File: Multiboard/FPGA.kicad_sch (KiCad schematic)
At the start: 0 parts

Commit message: Implemented FTDI in schematic
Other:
- added sheet FTDI (FT2232HL.kicad_sch)
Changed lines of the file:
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@@
 	(generator_version "9.0")
 	(paper "A4")
+	(sheet
+		(at 24.13 98.806)
+		(size 49.53 90.424)
+		(exclude_from_sim no)
+		(in_bom yes)
+		(on_board yes)
+		(dnp no)
+		(fields_autoplaced yes)
+		(stroke
+			(width 0.1524)
+			(type solid)
+		)
+		(fill
+			(color 0 0 0 0.0000)
+		)
+		(property "Sheetname" "FTDI"
+			(at 24.13 98.0944 0)
+			(effects
+				(font
+					(size 1.27 1.27)
+				)
+				(justify left bottom)
+			)
+		)
+		(property "Sheetfile" "FT2232HL.kicad_sch"
+			(at 24.13 189.8146 0)
+			(effects
+				(font
+					(size 1.27 1.27)
+				)
+				(justify left top)
+			)
+		)
+		(instances
+			(project "Multiboard"
+				(path "/9ed4a389-3aa7-41f1-b239-280eb7f09ef1/a1879700-d4ae-4f4f-b9ed-53e5618d969d"
+					(page "5")
+				)
+			)
+		)
+	)
 )

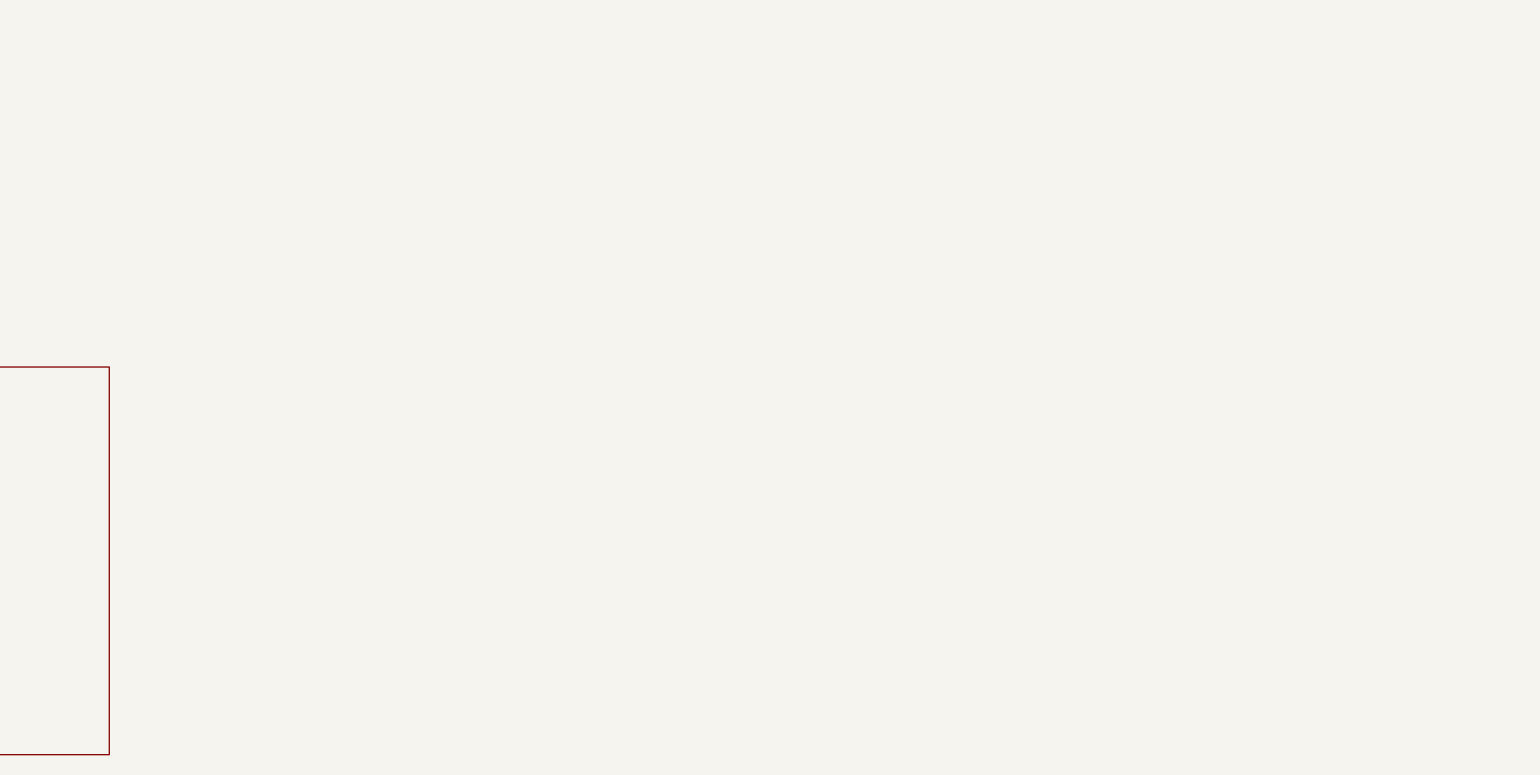
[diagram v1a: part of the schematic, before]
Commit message: added and wired banks to the fpga schematic
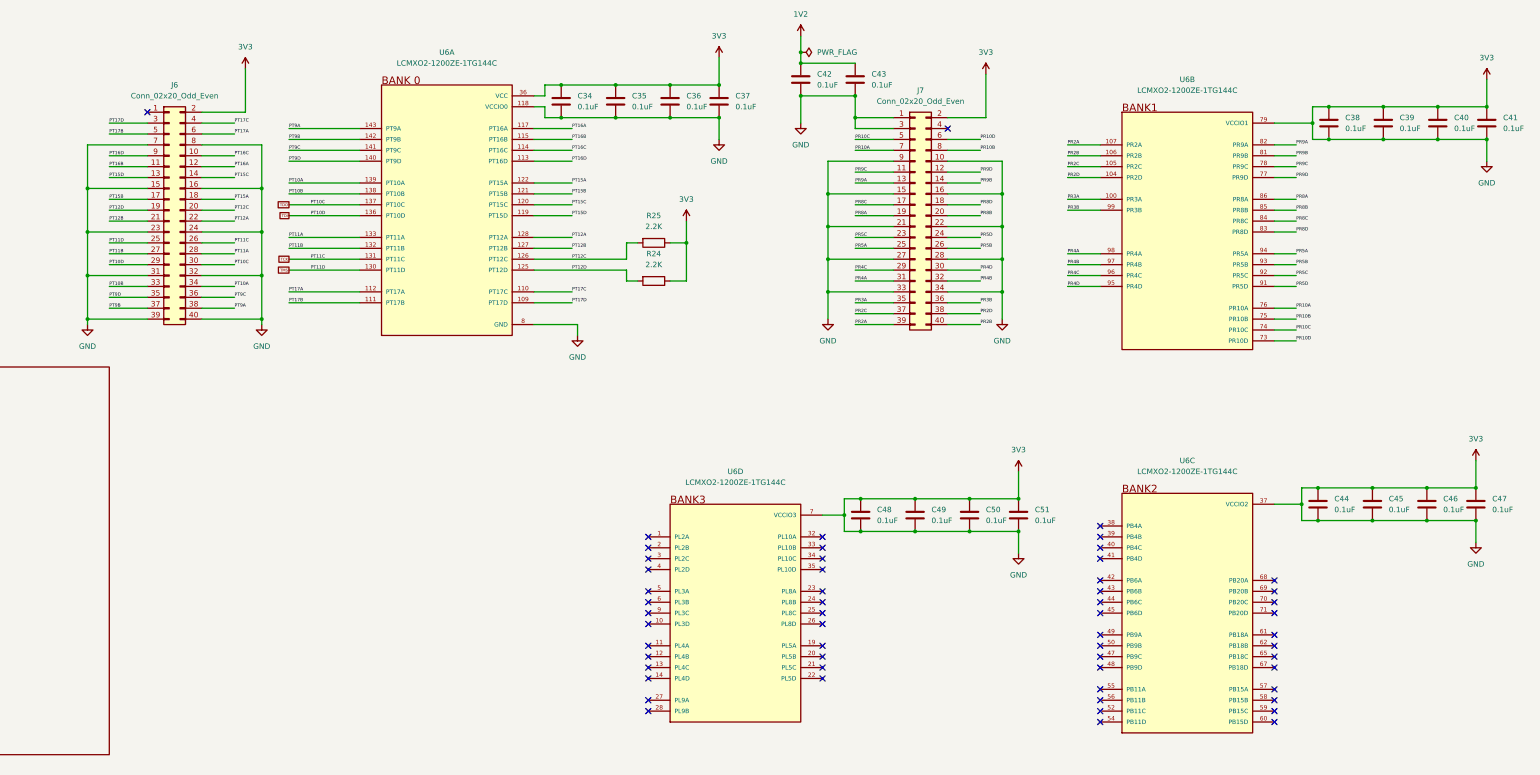
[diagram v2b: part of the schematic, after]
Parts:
- added C34, C35, C36, C37, C38, C39, C40, C41, C42, C43, C44, C45, C46, C47, C48, C49, C50, C51: 0.1uF, symbol Device:C
- added J6, J7: Conn_02x20_Odd_Even, Connector_IDC:IDC-Header_2x20_P2.54mm_Vertical, symbol Connector_Generic:Conn_02x20_Odd_Even
- added R24, R25: 2.2K, symbol Device:R
- added U6: LCMXO2-1200ZE-1TG144C, LCMXO2-1200ZE-1TG144C:QFP50P2200X2200X160-144N, symbol LCMXO2-1200ZE-1TG144C:LCMXO2-1200ZE-1TG144C
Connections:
- new net 1V2: C42.1, C43.1
- new net 3V3: C34.1, C34.2, C35.1, C35.2, C36.1, C36.2, C37.1, C37.2, C38.1, C38.2, C39.1, C39.2, C40.1, C40.2, C41.1, C41.2, C42.2, C43.2, C44.1, C44.2, C45.1, C45.2, C46.1, C46.2, C47.1, C47.2, C48.1, C48.2, C49.1, C49.2, C50.1, C50.2, C51.1, C51.2, J6.15 (Pin_15), J6.16 (Pin_16), J6.2 (Pin_2), J6.23 (Pin_23), J6.24 (Pin_24), J6.31 (Pin_31), J6.32 (Pin_32), J6.39 (Pin_39), J6.40 (Pin_40), J6.7 (Pin_7), J6.8 (Pin_8), J7.1 (Pin_1), J7.10 (Pin_10), J7.15 (Pin_15), J7.16 (Pin_16), J7.2 (Pin_2), J7.21 (Pin_21), J7.22 (Pin_22), J7.27 (Pin_27), J7.28 (Pin_28), J7.3 (Pin_3), J7.33 (Pin_33), J7.34 (Pin_34), J7.9 (Pin_9), R24.1, R25.1, U6.101 (GND), U6.102 (VCCIO1), U6.108 (VCC), U6.116 (GND), U6.118 (VCCIO0), U6.123 (VCCIO0), U6.124 (GND), U6.134 (GND), U6.135 (VCCIO0), U6.144 (VCC), U6.16 (VCCIO3), U6.18 (GND), U6.29 (GND), U6.30 (VCCIO3), U6.36 (VCC), U6.37 (VCCIO2), U6.46 (GND), U6.51 (VCCIO2), U6.53 (GND), U6.64 (GND), U6.66 (VCCIO2), U6.7 (VCCIO3), U6.72 (VCC), U6.79 (VCCIO1), U6.8 (GND), U6.80 (GND), U6.88 (VCCIO1), U6.90 (GND)
- new net PR10A: J7.7 (Pin_7), U6.76 (PR10A)
- new net PR10B: J7.8 (Pin_8), U6.75 (PR10B)
- new net PR10C: J7.5 (Pin_5), U6.74 (PR10C)
- new net PR10D: J7.6 (Pin_6), U6.73 (PR10D)
- new net PR2A: J7.39 (Pin_39), U6.107 (PR2A)
- new net PR2B: J7.40 (Pin_40), U6.106 (PR2B)
- new net PR2C: J7.37 (Pin_37), U6.105 (PR2C)
- new net PR2D: J7.38 (Pin_38), U6.104 (PR2D)
- new net PR3A: J7.35 (Pin_35), U6.100 (PR3A)
- new net PR3B: J7.36 (Pin_36), U6.99 (PR3B)
- new net PR4A: J7.31 (Pin_31), U6.98 (PR4A)
- new net PR4B: J7.32 (Pin_32), U6.97 (PR4B)
- new net PR4C: J7.29 (Pin_29), U6.96 (PR4C)
- new net PR4D: J7.30 (Pin_30), U6.95 (PR4D)
- new net PR5A: J7.25 (Pin_25), U6.94 (PR5A)
- new net PR5B: J7.26 (Pin_26), U6.93 (PR5B)
- new net PR5C: J7.23 (Pin_23), U6.92 (PR5C)
- new net PR5D: J7.24 (Pin_24), U6.91 (PR5D)
- new net PR8A: J7.19 (Pin_19), U6.86 (PR8A)
- new net PR8B: J7.20 (Pin_20), U6.85 (PR8B)
- new net PR8C: J7.17 (Pin_17), U6.84 (PR8C)
- new net PR8D: J7.18 (Pin_18), U6.83 (PR8D)
- new net PR9A: J7.13 (Pin_13), U6.82 (PR9A)
- new net PR9B: J7.14 (Pin_14), U6.81 (PR9B)
- new net PR9C: J7.11 (Pin_11), U6.78 (PR9C)
- new net PR9D: J7.12 (Pin_12), U6.77 (PR9D)
- new net PT10A: J6.34 (Pin_34), U6.139 (PT10A)
- new net PT10B: J6.33 (Pin_33), U6.138 (PT10B)
- new net PT11A: J6.28 (Pin_28), U6.133 (PT11A)
- new net PT11B: J6.27 (Pin_27), U6.132 (PT11B)
- new net PT12A: J6.22 (Pin_22), U6.128 (PT12A)
- new net PT12B: J6.21 (Pin_21), U6.127 (PT12B)
- new net PT12C: J6.20 (Pin_20), R25.2, U6.126 (PT12C)
- new net PT12D: J6.19 (Pin_19), R24.2, U6.125 (PT12D)
- new net PT15A: J6.18 (Pin_18), U6.122 (PT15A)
- new net PT15B: J6.17 (Pin_17), U6.121 (PT15B)
- new net PT15C: J6.14 (Pin_14), U6.120 (PT15C)
- new net PT15D: J6.13 (Pin_13), U6.119 (PT15D)
- new net PT16A: J6.12 (Pin_12), U6.117 (PT16A)
- new net PT16B: J6.11 (Pin_11), U6.115 (PT16B)
- new net PT16C: J6.10 (Pin_10), U6.114 (PT16C)
- new net PT16D: J6.9 (Pin_9), U6.113 (PT16D)
- new net PT17A: J6.6 (Pin_6), U6.112 (PT17A)
- new net PT17B: J6.5 (Pin_5), U6.111 (PT17B)
- new net PT17C: J6.4 (Pin_4), U6.110 (PT17C)
- new net PT17D: J6.3 (Pin_3), U6.109 (PT17D)
- new net PT9A: J6.38 (Pin_38), U6.143 (PT9A)
- new net PT9B: J6.37 (Pin_37), U6.142 (PT9B)
- new net PT9C: J6.36 (Pin_36), U6.141 (PT9C)
- new net PT9D: J6.35 (Pin_35), U6.140 (PT9D)
- new net TCK: J6.26 (Pin_26), U6.131 (PT11C)
- new net TDI: J6.29 (Pin_29), U6.136 (PT10D)
- new net TDO: J6.30 (Pin_30), U6.137 (PT10C)
- new net TMS: J6.25 (Pin_25), U6.130 (PT11D)
- no-connect marks 0 -> 56

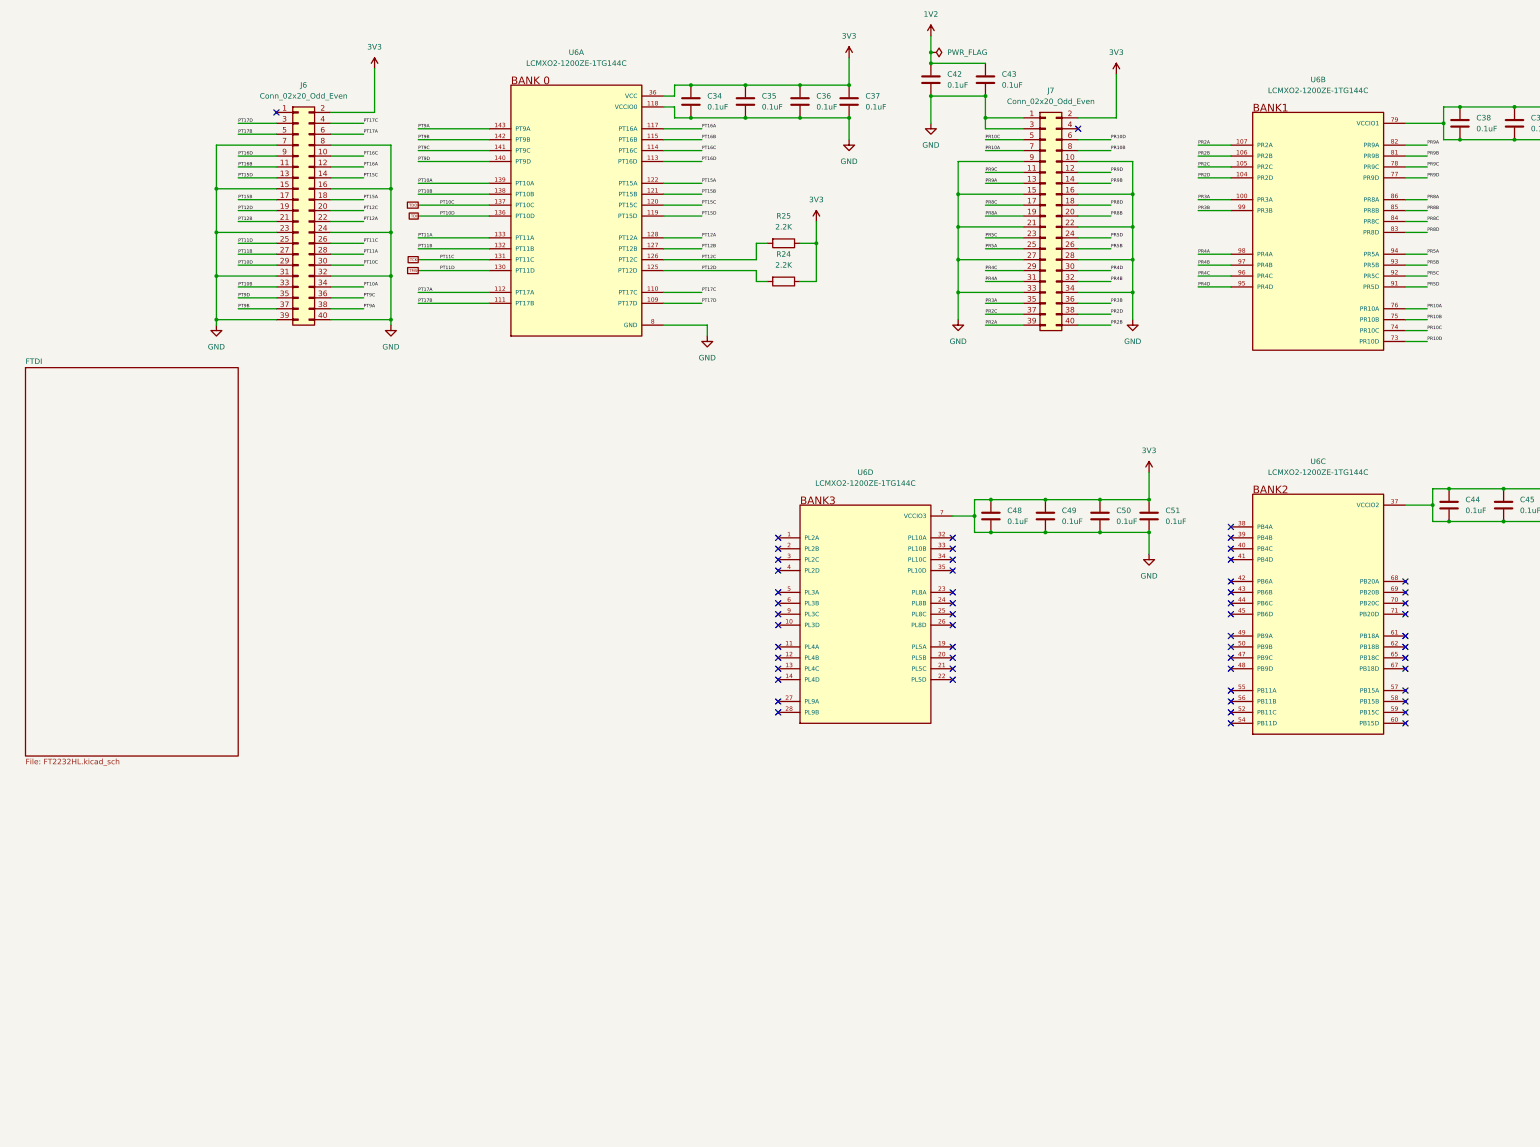
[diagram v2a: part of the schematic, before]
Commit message: completed v1 FPGA schematic
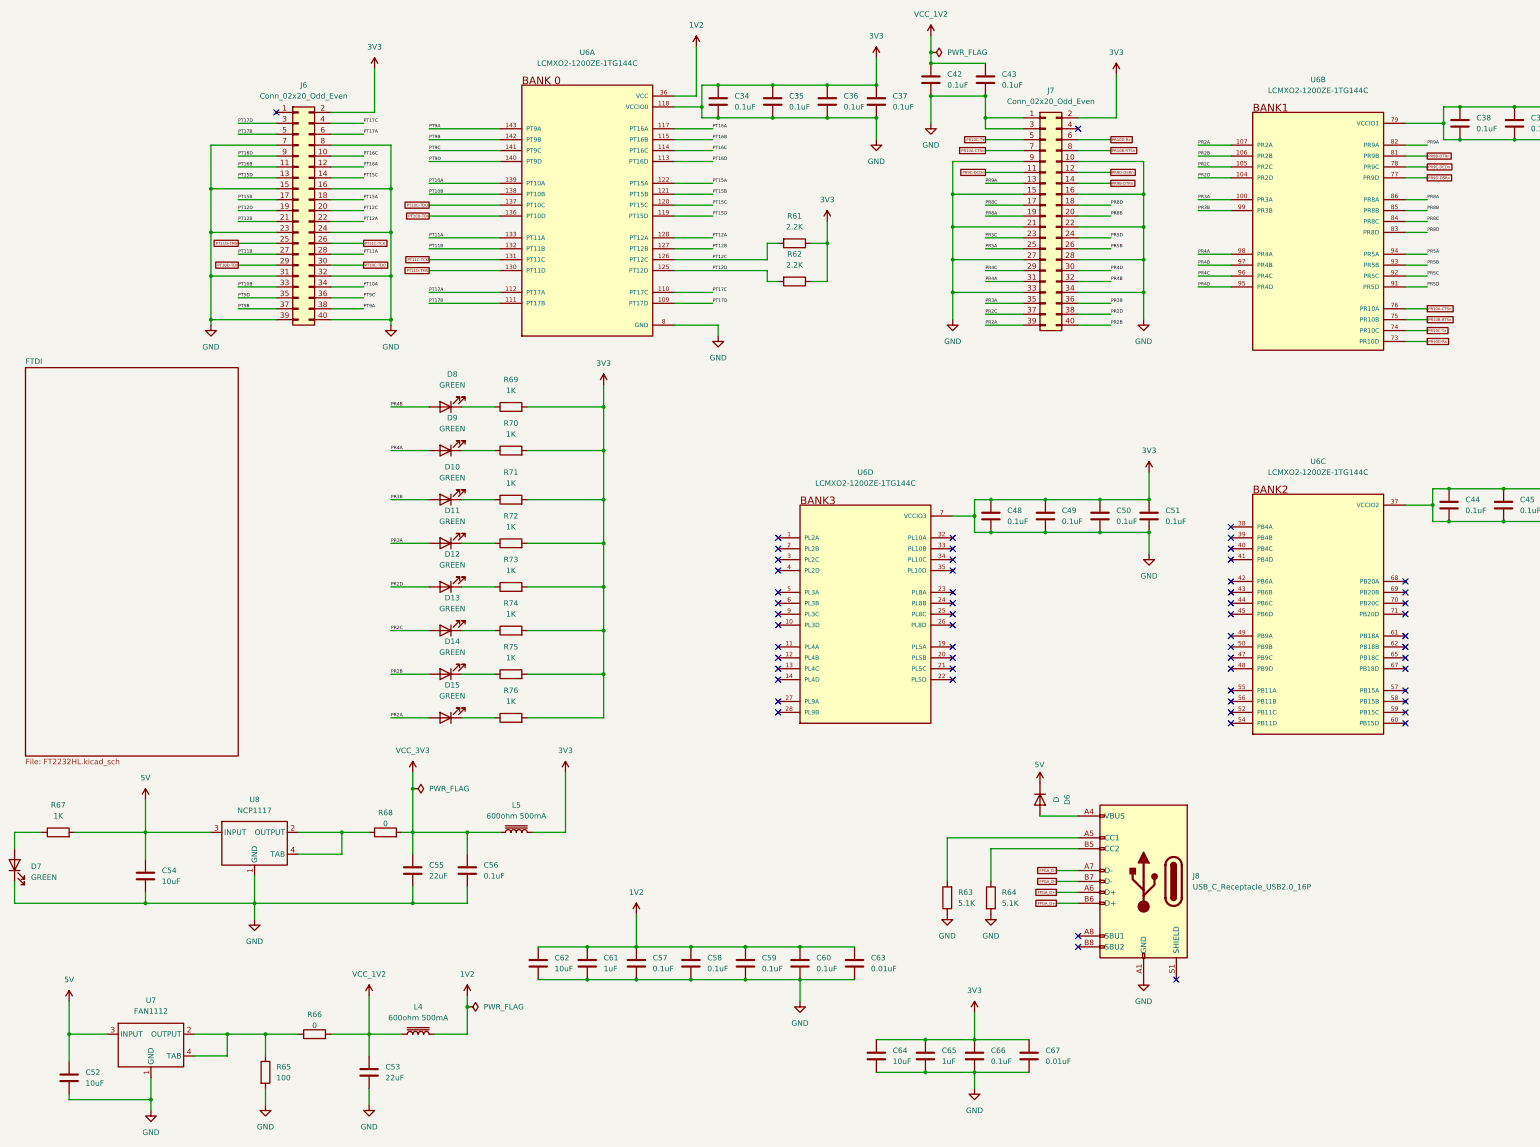
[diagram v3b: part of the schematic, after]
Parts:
- added C52, C54, C62, C64: 10uF, symbol Device:C
- added C53, C55: 22uF, symbol Device:C
- added C56, C57, C58, C59, C60, C66: 0.1uF, symbol Device:C
- added C61, C65: 1uF, symbol Device:C
- added C63, C67: 0.01uF, symbol Device:C
- added D10, D11, D12, D13, D14, D15, D7, D8, D9: GREEN, symbol Device:LED
- added D6: D, Diode_SMD:D_0603_1608Metric_Pad1.05x0.95mm_HandSolder, symbol Device:D
- added J8: USB_C_Receptacle_USB2.0_16P, Connector_USB:USB_C_Receptacle_G-Switch_GT-USB-7010ASV, symbol Connector:USB_C_Receptacle_USB2.0_16P
- added L4, L5: 600ohm 500mA, Inductor_SMD:L_0603_1608Metric_Pad1.05x0.95mm_HandSolder, symbol Device:L_Iron
- added R63, R64: 5.1K, symbol Device:R
- added R65: 100, symbol Device:R
- added R66, R68: 0, symbol Device:R
- added R67, R69, R70, R71, R72, R73, R74, R75, R76: 1K, symbol Device:R
- added U7: FAN1112, symbol FPGA_LDO:FPGA_LDO
- added U8: NCP1117, symbol FPGA_LDO:FPGA_LDO
- renumbered R25 to R61, R24 to R62
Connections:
- net 1V2: now also U6.108 (VCC), U6.144 (VCC), U6.36 (VCC), U6.72 (VCC), C57.1, C58.1, C59.1, C60.1, C61.1, C62.1, C63.1, L4.2; no longer C42.1, C43.1
- net 3V3: now also C52.2, C53.2, C54.2, C55.2, C56.2, C57.2, C58.2, C59.2, C60.2, C61.2, C62.2, C63.2, C64.1, C64.2, C65.1, C65.2, C66.1, C66.2, C67.1, C67.2, D7.1 (K), J8.A1 (GND), J8.A12 (GND), J8.B1 (GND), J8.B12 (GND), L5.2, R63.1, R64.2, R65.2, R69.2, R70.2, R71.2, R72.2, R73.2, R74.2, R75.2, R76.2, U7.1 (GND), U8.1 (GND); no longer U6.108 (VCC), U6.144 (VCC), U6.36 (VCC), U6.72 (VCC)
- net PR2A: now also D15.2 (A)
- net PR2B: now also D14.2 (A)
- net PR2C: now also D13.2 (A)
- net PR2D: now also D12.2 (A)
- net PR3A: now also D11.2 (A)
- net PR3B: now also D10.2 (A)
- net PR4A: now also D9.2 (A)
- net PR4B: now also D8.2 (A)
- net PR10A renamed PR10A-CTSn
- net PR10B renamed PR10B-RTSn
- net PR10C renamed PR10C-Tx
- net PR10D renamed PR10D-Rx
- net PR9B renamed PR9B-DTRn
- net PR9C renamed PR9C-DCDn
- net PR9D renamed PR9D-DSRn
- net TCK renamed PT11C-TCK
- net TDI renamed PT10D-TDI
- net TDO renamed PT10C-TDO
- net TMS renamed PT11D-TMS
- new net: D15.1 (K), R76.1
- new net: D13.1 (K), R74.1
- new net: R65.1, R66.1, U7.2 (OUTPUT), U7.4 (TAB)
- new net: D9.1 (K), R70.1
- new net: D6.2 (A), J8.A4 (VBUS), J8.A9 (VBUS), J8.B4 (VBUS), J8.B9 (VBUS)
- new net: D10.1 (K), R71.1
- new net: D14.1 (K), R75.1
- new net: D8.1 (K), R69.1
- new net: J8.A5 (CC1), R63.2
- new net: R68.1, U8.2 (OUTPUT), U8.4 (TAB)
- new net: D12.1 (K), R73.1
- new net: D7.2 (A), R67.1
- new net: D11.1 (K), R72.1
- new net: J8.B5 (CC2), R64.1
- new net 5V: C52.1, C54.1, D6.1 (K), R67.2, U7.3 (INPUT), U8.3 (INPUT)
- new net FPGA_D+: J8.A6 (D+), J8.B6 (D+)
- new net FPGA_D-: J8.A7 (D-), J8.B7 (D-)
- new net VCC_1V2: C42.1, C43.1, C53.1, L4.1, R66.2
- new net VCC_3V3: C55.1, C56.1, L5.1, R68.2
- no-connect marks 56 -> 59
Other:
- moved on the sheet: C34, C35, C36, C37, R61, R62, U6A
